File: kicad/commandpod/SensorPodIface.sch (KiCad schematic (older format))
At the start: 10 parts

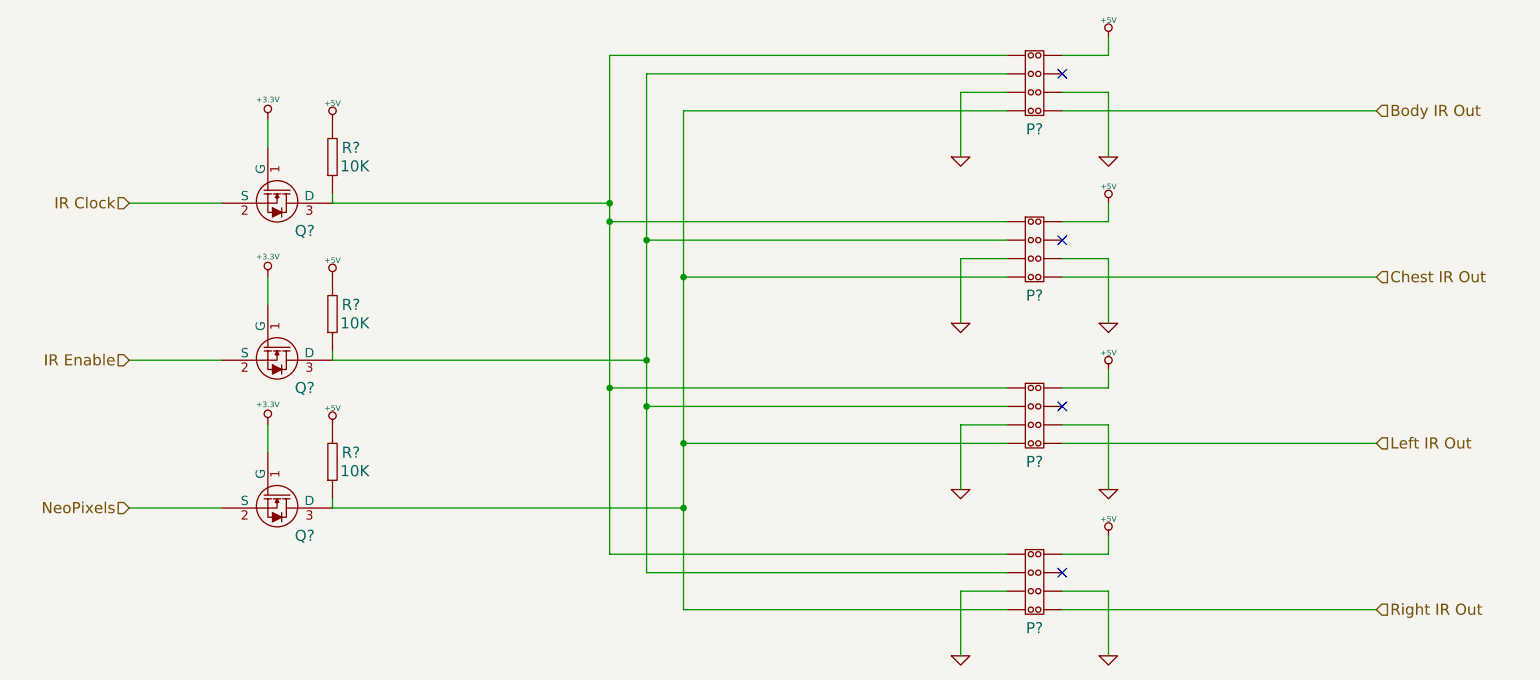
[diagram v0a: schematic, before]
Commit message: Annotated schematics
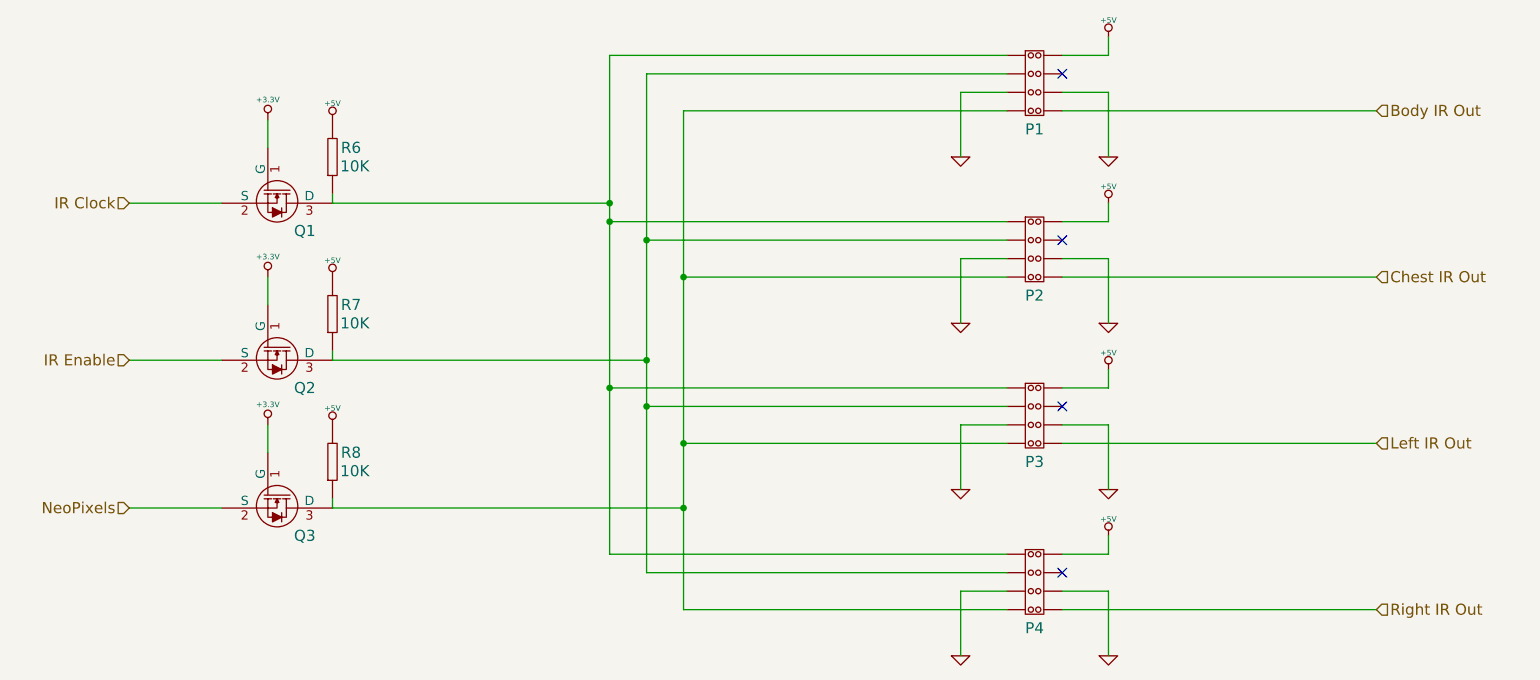
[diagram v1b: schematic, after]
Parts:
- gave numbers to parts that had none: 10
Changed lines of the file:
@@
 $EndDescr
 $Comp
-L IRFML8244TRPBF Q?
+L IRFML8244TRPBF Q2
 U 1 1 56D7CA74
 P 3100 4150
-F 0 "Q?" V 3250 4300 60  0000 C CNN
+F 0 "Q2" V 3250 4300 60  0000 C CNN
 F 1 "IRFML8244TRPBF" H 2350 3670 60  0001 C CNN
 F 2 "~" H 2300 4150 60  0000 C CNN
@@
 $EndComp
 $Comp
-L +3.3V #PWR?
+L +3.3V #PWR014
 U 1 1 56D7CA7A
 P 3050 3700
-F 0 "#PWR?" H 3050 3660 30  0001 C CNN
+F 0 "#PWR014" H 3050 3660 30  0001 C CNN
 F 1 "+3.3V" H 3050 3810 30  0000 C CNN
 F 2 "" H 3050 3700 60  0000 C CNN
@@
 $EndComp
 $Comp
-L +5V #PWR?
+L +5V #PWR015
 U 1 1 56D7CA80
 P 3400 3700
-F 0 "#PWR?" H 3400 3790 20  0001 C CNN
+F 0 "#PWR015" H 3400 3790 20  0001 C CNN
 F 1 "+5V" H 3400 3790 30  0000 C CNN
 F 2 "" H 3400 3700 60  0000 C CNN
@@
 $EndComp
 $Comp
-L GENERIC_RESISTOR R?
+L GENERIC_RESISTOR R7
 U 1 1 56D7CA87
 P 3400 3900
-F 0 "R?" V 3450 3800 60  0000 C CNN
+F 0 "R7" V 3450 3800 60  0000 C CNN
 F 1 "GENERIC_RESISTOR" H 3440 3680 60  0001 C CNN
 F 2 "~" H 3350 3650 60  0000 C CNN
@@
 $EndComp
 $Comp
-L IRFML8244TRPBF Q?
+L IRFML8244TRPBF Q1
 U 1 1 56D7CA8E
 P 3100 3300
-F 0 "Q?" V 3250 3450 60  0000 C CNN
+F 0 "Q1" V 3250 3450 60  0000 C CNN
 F 1 "IRFML8244TRPBF" H 2350 2820 60  0001 C CNN
 F 2 "~" H 2300 3300 60  0000 C CNN
@@
 $EndComp
 $Comp
-L +3.3V #PWR?
+L +3.3V #PWR016
 U 1 1 56D7CA94
 P 3050 2850
-F 0 "#PWR?" H 3050 2810 30  0001 C CNN
+F 0 "#PWR016" H 3050 2810 30  0001 C CNN
 F 1 "+3.3V" H 3050 2960 30  0000 C CNN
 F 2 "" H 3050 2850 60  0000 C CNN
@@
 $EndComp
 $Comp
-L +5V #PWR?
+L +5V #PWR017
 U 1 1 56D7CA9A
 P 3400 2850
-F 0 "#PWR?" H 3400 2940 20  0001 C CNN
+F 0 "#PWR017" H 3400 2940 20  0001 C CNN
 F 1 "+5V" H 3400 2940 30  0000 C CNN
 F 2 "" H 3400 2850 60  0000 C CNN
@@
 $EndComp
 $Comp
-L GENERIC_RESISTOR R?
+L GENERIC_RESISTOR R6
 U 1 1 56D7CAA1
 P 3400 3050
-F 0 "R?" V 3450 2950 60  0000 C CNN
+F 0 "R6" V 3450 2950 60  0000 C CNN
 F 1 "GENERIC_RESISTOR" H 3440 2830 60  0001 C CNN
 F 2 "~" H 3350 2800 60  0000 C CNN
@@
 $EndComp
 $Comp
-L IRFML8244TRPBF Q?
+L IRFML8244TRPBF Q3
 U 1 1 56D7CAA7
 P 3100 4950
-F 0 "Q?" V 3250 5100 60  0000 C CNN
+F 0 "Q3" V 3250 5100 60  0000 C CNN
 F 1 "IRFML8244TRPBF" H 2350 4470 60  0001 C CNN
 F 2 "~" H 2300 4950 60  0000 C CNN
@@
 $EndComp
 $Comp
-L +3.3V #PWR?
+L +3.3V #PWR018
 U 1 1 56D7CAAD
 P 3050 4500
-F 0 "#PWR?" H 3050 4460 30  0001 C CNN
+F 0 "#PWR018" H 3050 4460 30  0001 C CNN
 F 1 "+3.3V" H 3050 4610 30  0000 C CNN
 F 2 "" H 3050 4500 60  0000 C CNN
@@
 $EndComp
 $Comp
-L +5V #PWR?
+L +5V #PWR019
 U 1 1 56D7CAB3
 P 3400 4500
-F 0 "#PWR?" H 3400 4590 20  0001 C CNN
+F 0 "#PWR019" H 3400 4590 20  0001 C CNN
 F 1 "+5V" H 3400 4590 30  0000 C CNN
 F 2 "" H 3400 4500 60  0000 C CNN
@@
 $EndComp
 $Comp
-L GENERIC_RESISTOR R?
+L GENERIC_RESISTOR R8
 U 1 1 56D7CABA
 P 3400 4700
-F 0 "R?" V 3450 4600 60  0000 C CNN
+F 0 "R8" V 3450 4600 60  0000 C CNN
 F 1 "GENERIC_RESISTOR" H 3440 4480 60  0001 C CNN
 F 2 "~" H 3350 4450 60  0000 C CNN
@@
 	2300 4950 2800 4950
 $Comp
-L HEADER_(8_WAY) P?
+L HEADER_(8_WAY) P4
 U 1 1 56D7CE85
 P 7200 5300
-F 0 "P?" H 7200 5000 60  0000 C CNN
+F 0 "P4" H 7200 5000 60  0000 C CNN
 F 1 "HEADER_(8_WAY)" H 7200 5500 60  0001 C CNN
 F 2 "~" H 7250 5350 60  0000 C CNN
@@
 $EndComp
 $Comp
-L +5V #PWR?
+L +5V #PWR020
 U 1 1 56D7CE8B
 P 7600 5100
-F 0 "#PWR?" H 7600 5190 20  0001 C CNN
+F 0 "#PWR020" H 7600 5190 20  0001 C CNN
 F 1 "+5V" H 7600 5190 30  0000 C CNN
 F 2 "" H 7600 5100 60  0000 C CNN
@@
 $EndComp
 $Comp
-L GND #PWR?
+L GND #PWR021
 U 1 1 56D7CE91
 P 6800 5750
-F 0 "#PWR?" H 6800 5750 30  0001 C CNN
+F 0 "#PWR021" H 6800 5750 30  0001 C CNN
 F 1 "GND" H 6800 5680 30  0001 C CNN
 F 2 "" H 6800 5750 60  0000 C CNN
@@
 $EndComp
 $Comp
-L GND #PWR?
+L GND #PWR022
 U 1 1 56D7CE97
 P 7600 5750
-F 0 "#PWR?" H 7600 5750 30  0001 C CNN
+F 0 "#PWR022" H 7600 5750 30  0001 C CNN
 F 1 "GND" H 7600 5680 30  0001 C CNN
 F 2 "" H 7600 5750 60  0000 C CNN
@@
 $EndComp
 $Comp
-L HEADER_(8_WAY) P?
+L HEADER_(8_WAY) P3
 U 1 1 56D7CEA2
 P 7200 4400
-F 0 "P?" H 7200 4100 60  0000 C CNN
+F 0 "P3" H 7200 4100 60  0000 C CNN
 F 1 "HEADER_(8_WAY)" H 7200 4600 60  0001 C CNN
 F 2 "~" H 7250 4450 60  0000 C CNN
@@
 $EndComp
 $Comp
-L +5V #PWR?
+L +5V #PWR023
 U 1 1 56D7CEA8
 P 7600 4200
-F 0 "#PWR?" H 7600 4290 20  0001 C CNN
+F 0 "#PWR023" H 7600 4290 20  0001 C CNN
 F 1 "+5V" H 7600 4290 30  0000 C CNN
 F 2 "" H 7600 4200 60  0000 C CNN
@@
 $EndComp
 $Comp
-L GND #PWR?
+L GND #PWR024
 U 1 1 56D7CEAE
 P 6800 4850
-F 0 "#PWR?" H 6800 4850 30  0001 C CNN
+F 0 "#PWR024" H 6800 4850 30  0001 C CNN
 F 1 "GND" H 6800 4780 30  0001 C CNN
 F 2 "" H 6800 4850 60  0000 C CNN
@@
 $EndComp
 $Comp
-L GND #PWR?
+L GND #PWR025
 U 1 1 56D7CEB4
 P 7600 4850
-F 0 "#PWR?" H 7600 4850 30  0001 C CNN
+F 0 "#PWR025" H 7600 4850 30  0001 C CNN
 F 1 "GND" H 7600 4780 30  0001 C CNN
 F 2 "" H 7600 4850 60  0000 C CNN
@@
 $EndComp
 $Comp
-L +5V #PWR?
+L +5V #PWR026
 U 1 1 56D7CEC5
 P 7600 3300
-F 0 "#PWR?" H 7600 3390 20  0001 C CNN
+F 0 "#PWR026" H 7600 3390 20  0001 C CNN
 F 1 "+5V" H 7600 3390 30  0000 C CNN
 F 2 "" H 7600 3300 60  0000 C CNN
@@
 $EndComp
 $Comp
-L GND #PWR?
+L GND #PWR027
 U 1 1 56D7CECB
 P 6800 3950
-F 0 "#PWR?" H 6800 3950 30  0001 C CNN
+F 0 "#PWR027" H 6800 3950 30  0001 C CNN
 F 1 "GND" H 6800 3880 30  0001 C CNN
 F 2 "" H 6800 3950 60  0000 C CNN
@@
 $EndComp
 $Comp
-L GND #PWR?
+L GND #PWR028
 U 1 1 56D7CED1
 P 7600 3950
-F 0 "#PWR?" H 7600 3950 30  0001 C CNN
+F 0 "#PWR028" H 7600 3950 30  0001 C CNN
 F 1 "GND" H 7600 3880 30  0001 C CNN
 F 2 "" H 7600 3950 60  0000 C CNN
@@
 $EndComp
 $Comp
-L +5V #PWR?
+L +5V #PWR029
 U 1 1 56D7CEE2
 P 7600 2400
-F 0 "#PWR?" H 7600 2490 20  0001 C CNN
+F 0 "#PWR029" H 7600 2490 20  0001 C CNN
 F 1 "+5V" H 7600 2490 30  0000 C CNN
 F 2 "" H 7600 2400 60  0000 C CNN
@@
 $EndComp
 $Comp
-L GND #PWR?
+L GND #PWR030
 U 1 1 56D7CEE8
 P 6800 3050
-F 0 "#PWR?" H 6800 3050 30  0001 C CNN
+F 0 "#PWR030" H 6800 3050 30  0001 C CNN
 F 1 "GND" H 6800 2980 30  0001 C CNN
 F 2 "" H 6800 3050 60  0000 C CNN
@@
 $EndComp
 $Comp
-L GND #PWR?
+L GND #PWR031
 U 1 1 56D7CEEE
 P 7600 3050
-F 0 "#PWR?" H 7600 3050 30  0001 C CNN
+F 0 "#PWR031" H 7600 3050 30  0001 C CNN
 F 1 "GND" H 7600 2980 30  0001 C CNN
 F 2 "" H 7600 3050 60  0000 C CNN
@@
 Connection ~ 5300 3700
 $Comp
-L HEADER_(8_WAY) P?
+L HEADER_(8_WAY) P1
 U 1 1 56D7CEDC
 P 7200 2600
-F 0 "P?" H 7200 2300 60  0000 C CNN
+F 0 "P1" H 7200 2300 60  0000 C CNN
 F 1 "HEADER_(8_WAY)" H 7200 2800 60  0001 C CNN
 F 2 "~" H 7250 2650 60  0000 C CNN
@@
 $EndComp
 $Comp
-L HEADER_(8_WAY) P?
+L HEADER_(8_WAY) P2
 U 1 1 56D7CEBF
 P 7200 3500
-F 0 "P?" H 7200 3200 60  0000 C CNN
+F 0 "P2" H 7200 3200 60  0000 C CNN
 F 1 "HEADER_(8_WAY)" H 7200 3700 60  0001 C CNN
 F 2 "~" H 7250 3550 60  0000 C CNN
